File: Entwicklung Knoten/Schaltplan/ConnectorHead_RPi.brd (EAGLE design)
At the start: 65 x 64 mm, 45 parts, among them IC1 TINY24/44/84-PU, T1 2N7000, T2 2N7000, T3 2N7000, T4 2N7000, T5 2N7000, T8 2N7000

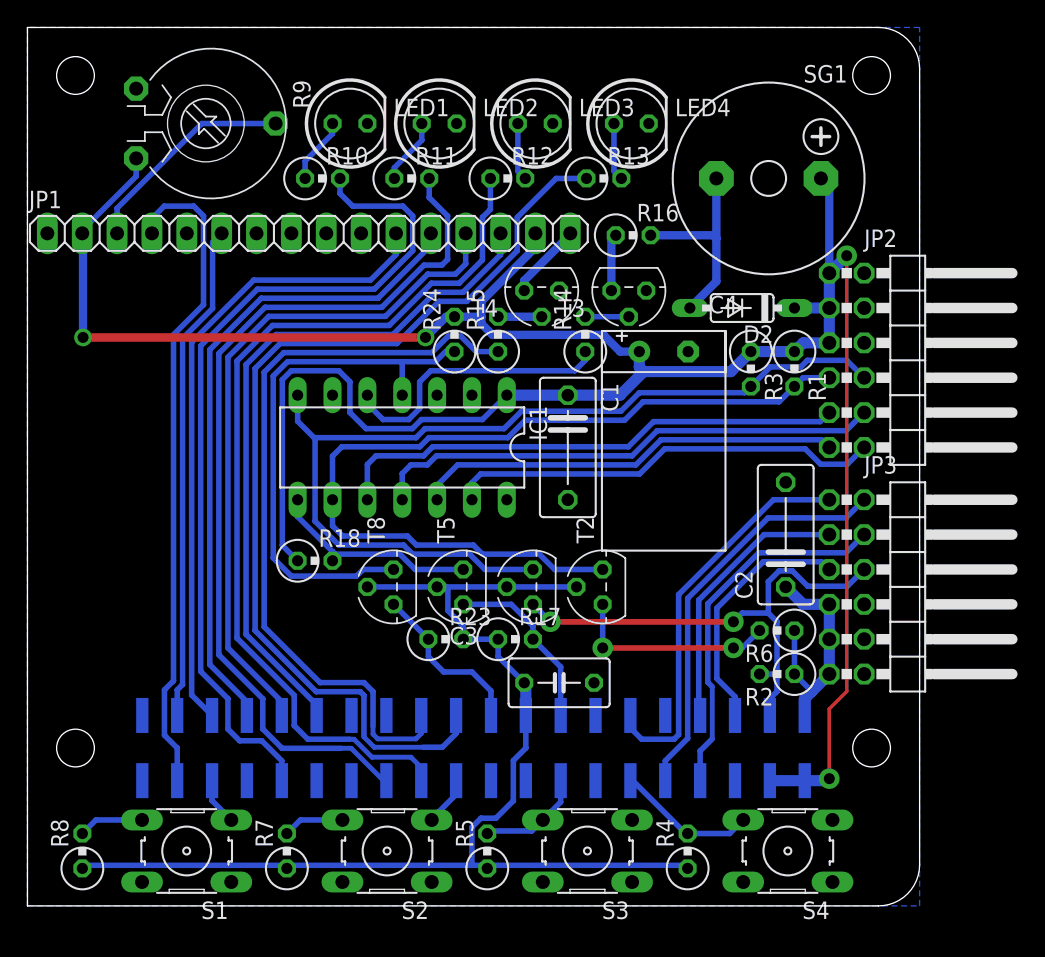
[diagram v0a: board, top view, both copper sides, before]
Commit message: Prototypen angepasst - LED Pads vergrößert, um Lösen durch Hebelwirkung zu vermeiden - Pads des Potentiometer vergrößert - Widerstände der Taster angepasst, da es durch leichte Kriechströme zu Verschiebungen kam - Widerstände gegen Masse auf der Sound-Signal, sowie Display-Backlight Leitung hinzugefügt, damit der Floating-Zustand beim Booten des Raspberry Pi's keine ungewollten Effekte auslöst
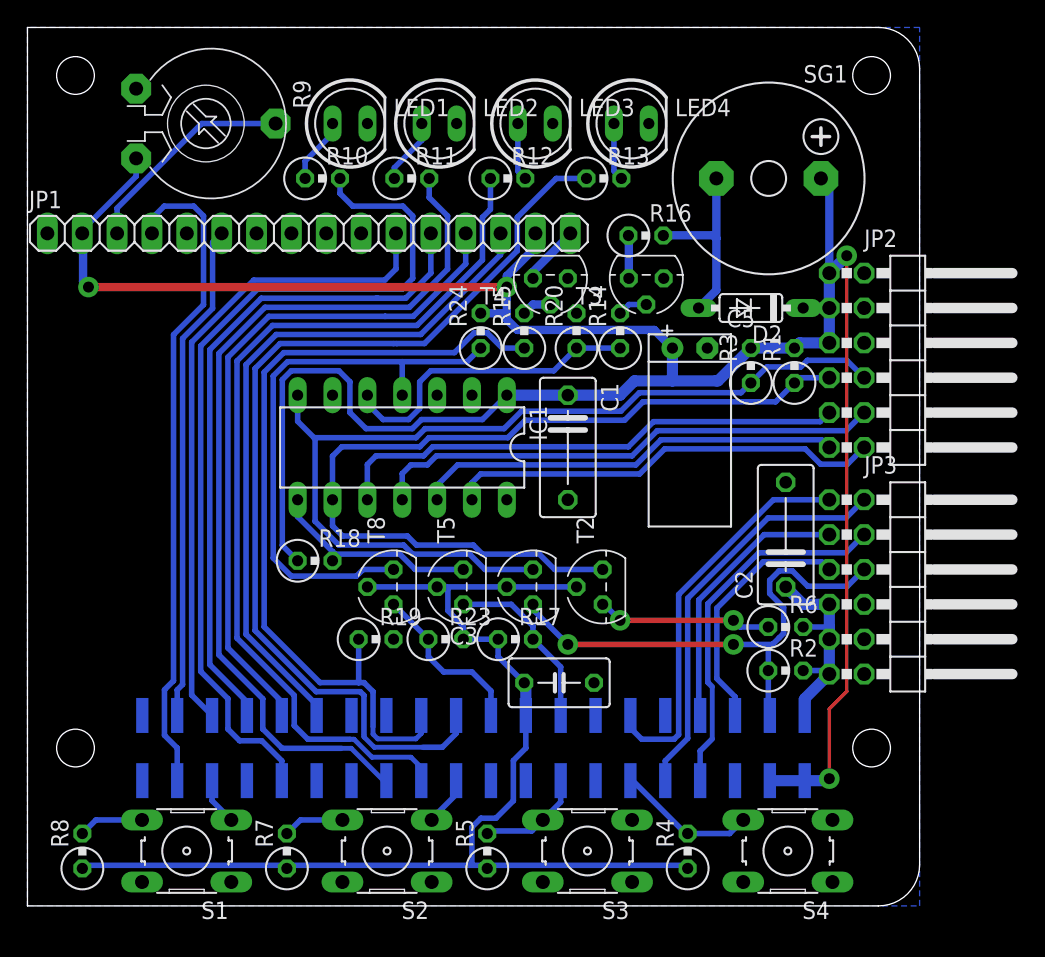
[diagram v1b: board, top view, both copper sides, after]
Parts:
- removed C4: 680µF/16V, rcl:E3,5-8_FLAT_DOWN
- added C5: 100uF/16V, rcl:E2,5-6_FLAT_DOWN
- added R19, R20: 10k, rcl:0309V
- R4, R5, R7, R8: value 10k -> 1k
- moved R14 2.55 mm to (43.2, 41.9)
- moved R24 1.92 mm to (33.0, 41.9)
- moved R15 1.92 mm to (36.2, 41.9)
- moved T3 1.55 mm to (45.1, 45.7)
- moved T4 1.09 mm to (38.1, 45.7)
- moved R16 0.92 mm to (45.1, 48.8)
- moved R2 0.68 mm to (55.2, 17.1), turned to 0 degrees
- moved R6 0.68 mm to (55.2, 20.3), turned to 0 degrees
- moved D2 0.63 mm to (52.7, 43.6)
- moved R1 0.25 mm to (55.9, 39.4), turned to 90 degrees
- moved R3 0.25 mm to (52.7, 39.4), turned to 90 degrees
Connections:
- net +3V3: now also R2.2, R6.2; no longer R2.1, R6.1
- net +5V: now also C5.+, R1.2, R3.2; no longer C4.+, R1.1, R3.1
- net DSP_BL: now also R19.1
- net GND: now also C5.-, R19.2, R20.2; no longer C4.-
- net I2C_SCL_3V3: now also R6.1; no longer R6.2
- net I2C_SCL_5V: now also R1.1; no longer R1.2
- net I2C_SDA_3V3: now also R2.1; no longer R2.2
- net I2C_SDA_5V: now also R3.1; no longer R3.2
- net SOUND_SIG: now also R20.1
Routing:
- net DSP_BL: track 55.3 -> 60.4 mm
- net I2C_SCL_3V3: track 34.5 -> 32.2 mm
- net SOUND_SIG: track 20.5 -> 22.8 mm
- net UC_RESET_5V: track 39.2 -> 41.2 mm
- net LED_B: track 63.0 -> 64.2 mm
- net DSP_D5: track 47.9 -> 49.1 mm
- net N$6: track 15.1 -> 13.9 mm
- net DSP_BL_GND: track 5.56 -> 4.41 mm
- net +5V: track 185.5 -> 184.4 mm
- net +3V3: track 103.9 -> 102.8 mm
- net N$5: track 4.16 -> 3.13 mm
- net N$9: track 3.18 -> 2.17 mm
- net N$7: track 3.17 -> 2.17 mm
- net DSP_D4: track 46.9 -> 47.5 mm
